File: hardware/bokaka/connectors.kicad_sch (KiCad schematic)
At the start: 3 parts, among them J1 USB_C_Receptacle_USB2.0_16P

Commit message: Adding rest of design and pdf
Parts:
- added J2: Tap Connector, symbol Connector:Conn_01x05_Pin
- added J3: SWD Connector, Connector:Tag-Connect_TC2030-IDC-NL_2x03_P1.27mm_Vertical, symbol Connector:Conn_ARM_SWD_TagConnect_TC2030-NL
- added J4: Conn_01x02_Pin, symbol Connector:Conn_01x02_Pin
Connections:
- net GND: now also J2.1 (Pin_1), J3.5 (GND)
- new net +3V3: J3.1 (VCC)
- new net I2C_SCL: J4.2 (Pin_2)
- new net I2C_SDA: J4.1 (Pin_1)
- new net SWD_SWCLK: J3.4 (SWCLK)
- new net SWD_SWDIO: J3.2 (SWDIO)
- new net TAP_DATA: J2.2 (Pin_2)
- new net TAP_DETECT: J2.3 (Pin_3)
- new net UART_RX: J2.4 (Pin_4)
- new net UART_TX: J2.5 (Pin_5)
- new net ~{RESET}: J3.3 (~{RESET})
- no-connect marks 2 -> 3

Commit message: Finalize design before pcb
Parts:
- removed J2: Tap Connector, symbol Connector:Conn_01x05_Pin
- added J2: Conn_01x02_Pin, symbol Connector:Conn_01x02_Pin
- added J5, J6: Conn_01x03_Pin, symbol Connector:Conn_01x03_Pin
- added U4: PESD5V0L4UG_115, Footprints:SOT65P210X110-5N, symbol Symbols:PESD5V0L4UG_115
- J3: footprint Connector:Tag-Connect_TC2030-IDC-NL_2x03_P1.27mm_Vertical -> Footprints:Edge_Connect_6
- R2, R3: footprint (none) -> Resistor_SMD:R_0402_1005Metric
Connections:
- net GND: now also J5.1 (Pin_1), J6.3 (Pin_3), U4.2
- net TAP_DATA: now also J5.3 (Pin_3), J6.1 (Pin_1), U4.4
- net TAP_DETECT: now also J5.2 (Pin_2), J6.2 (Pin_2), U4.5
- net UART_RX: now also J2.1 (Pin_1)
- net UART_TX: now also J2.2 (Pin_2)
- net USB_D-: now also U4.1, U4.3
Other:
- note added: "ESD Protection"
- moved on the sheet: J3

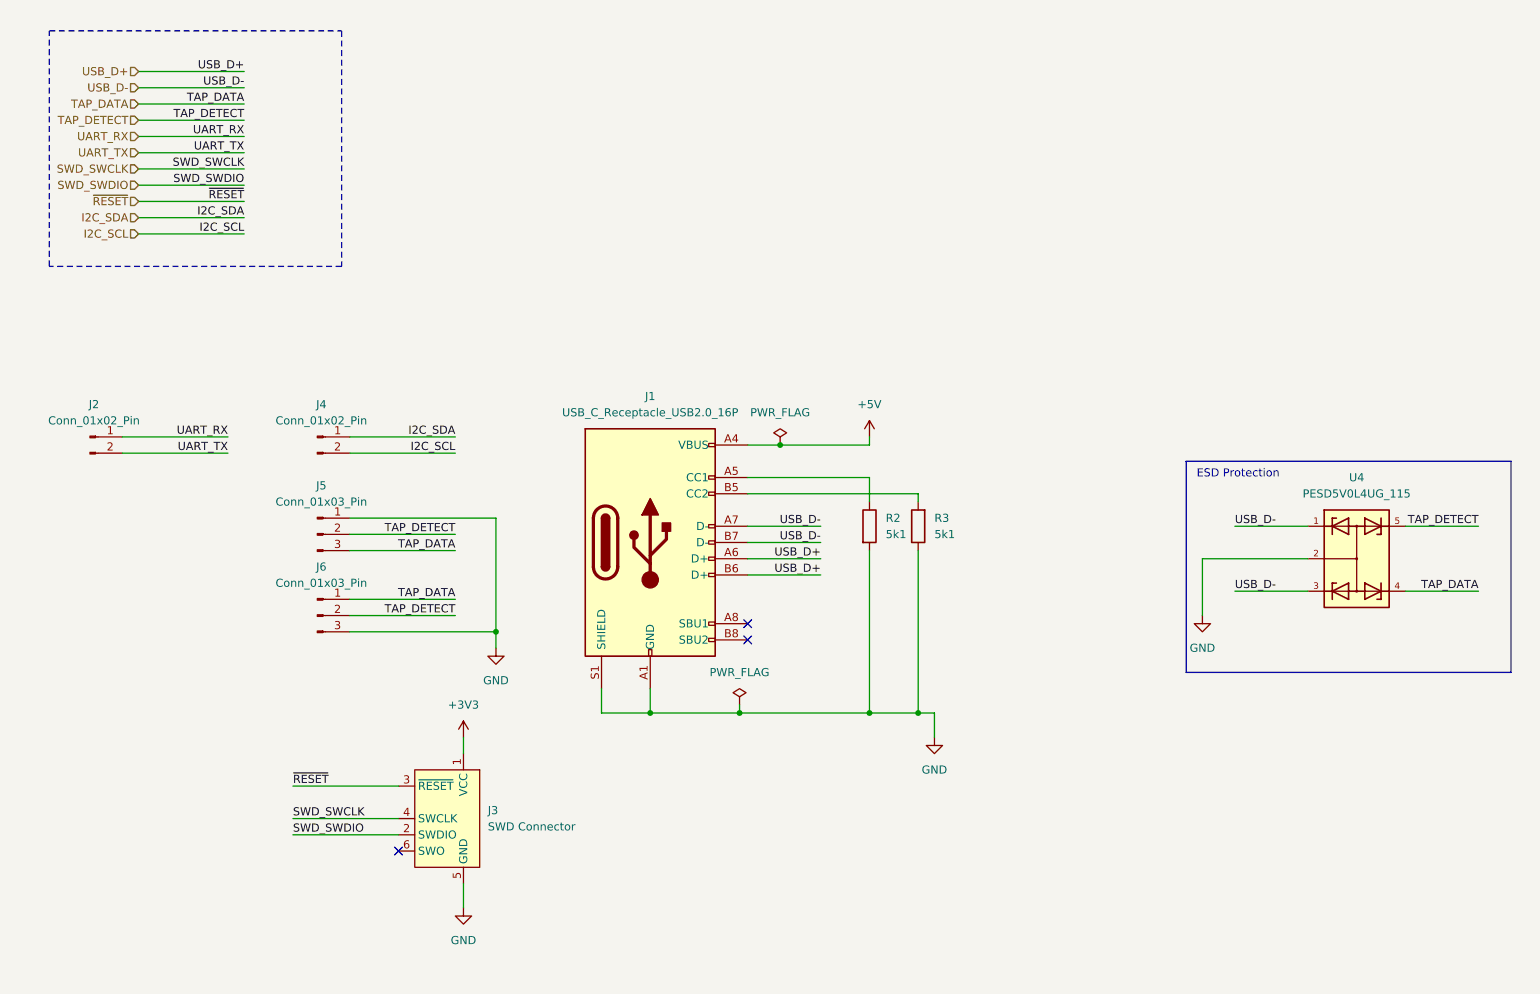
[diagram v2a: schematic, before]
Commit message: footprint asignment
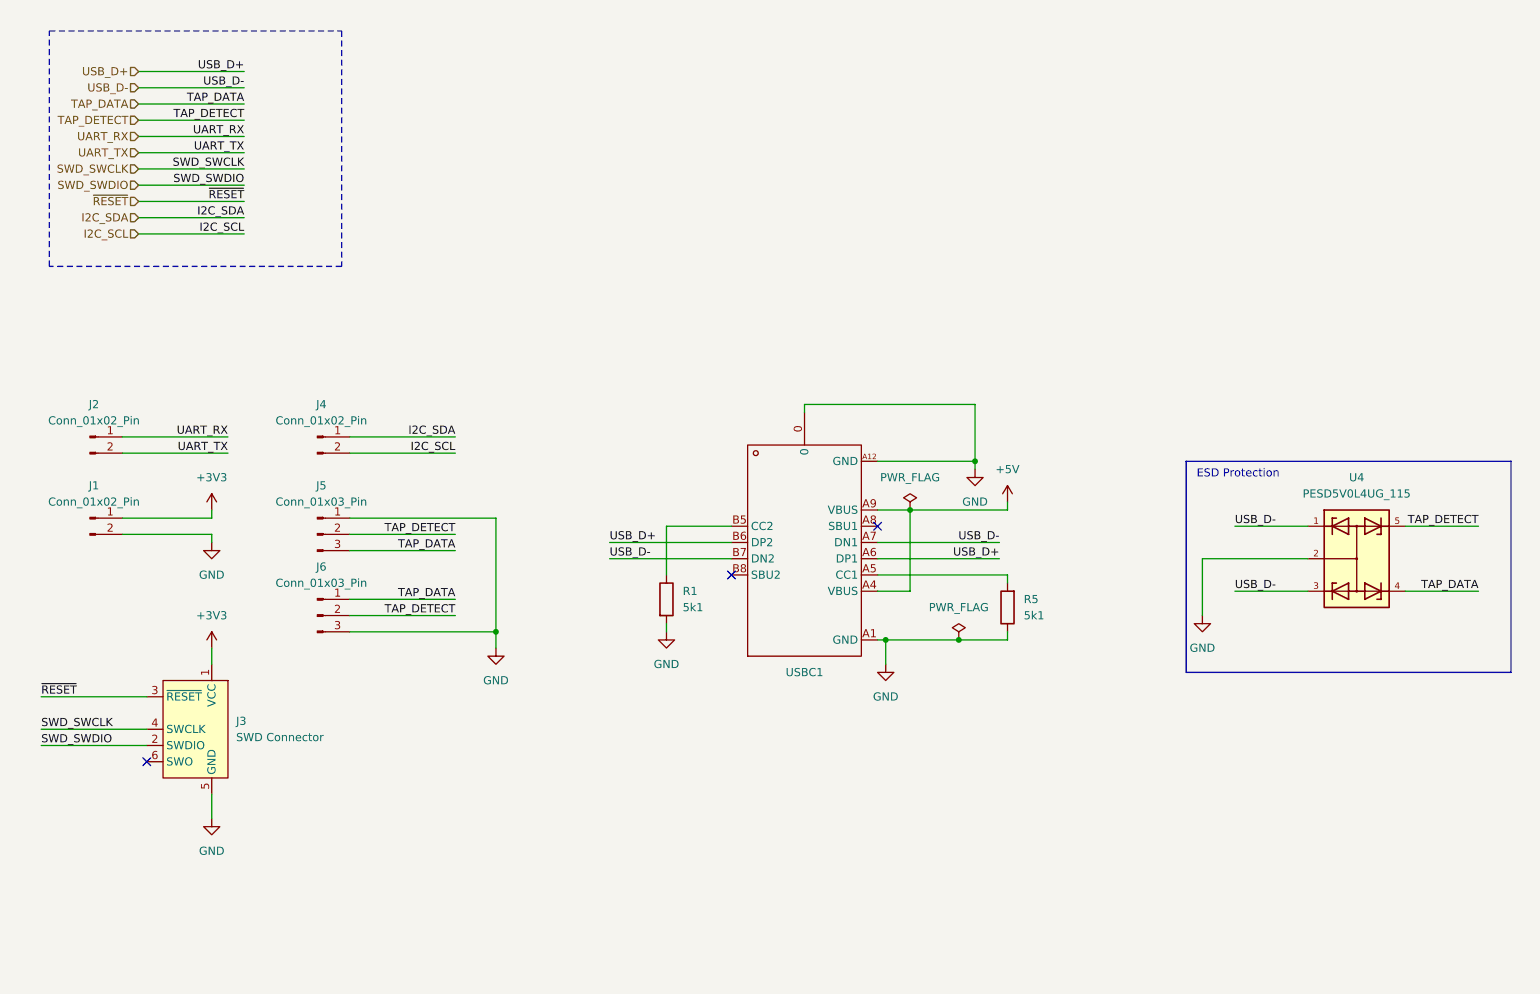
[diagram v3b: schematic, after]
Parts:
- removed J1: USB_C_Receptacle_USB2.0_16P, symbol Connector:USB_C_Receptacle_USB2.0_16P
- removed R2, R3: 5k1, Resistor_SMD:R_0402_1005Metric, symbol Device:R
- added J1: Conn_01x02_Pin, Connector_PinHeader_2.54mm:PinHeader_1x02_P2.54mm_Vertical, symbol Connector:Conn_01x02_Pin
- added R1, R5: 5k1, Resistor_SMD:R_0402_1005Metric, symbol Device:R
- added USBC1: ~, EasyEDA_Lib:USB-C-SMD_TYPE-C-USB-17, symbol Symbols:USB3.1C16PFSMT
- J2, J4: footprint (none) -> Connector_PinHeader_2.54mm:PinHeader_1x02_P2.54mm_Vertical
- J5, J6: footprint (none) -> Connector_PinHeader_2.54mm:PinHeader_1x03_P2.54mm_Vertical
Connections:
- net +3V3: now also J1.1 (Pin_1)
- net +5V: now also USBC1.A4 (VBUS), USBC1.A9 (VBUS)
- net GND: now also J1.2 (Pin_2), R1.2, R5.1, USBC1.0, USBC1.A1 (GND), USBC1.A12 (GND)
- net USB_D+: now also USBC1.A6 (DP1), USBC1.B6 (DP2)
- net USB_D-: now also USBC1.A7 (DN1), USBC1.B7 (DN2)
- new net: R1.1, USBC1.B5 (CC2)
- new net: R5.2, USBC1.A5 (CC1)
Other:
- moved on the sheet: J3

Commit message: schematic update
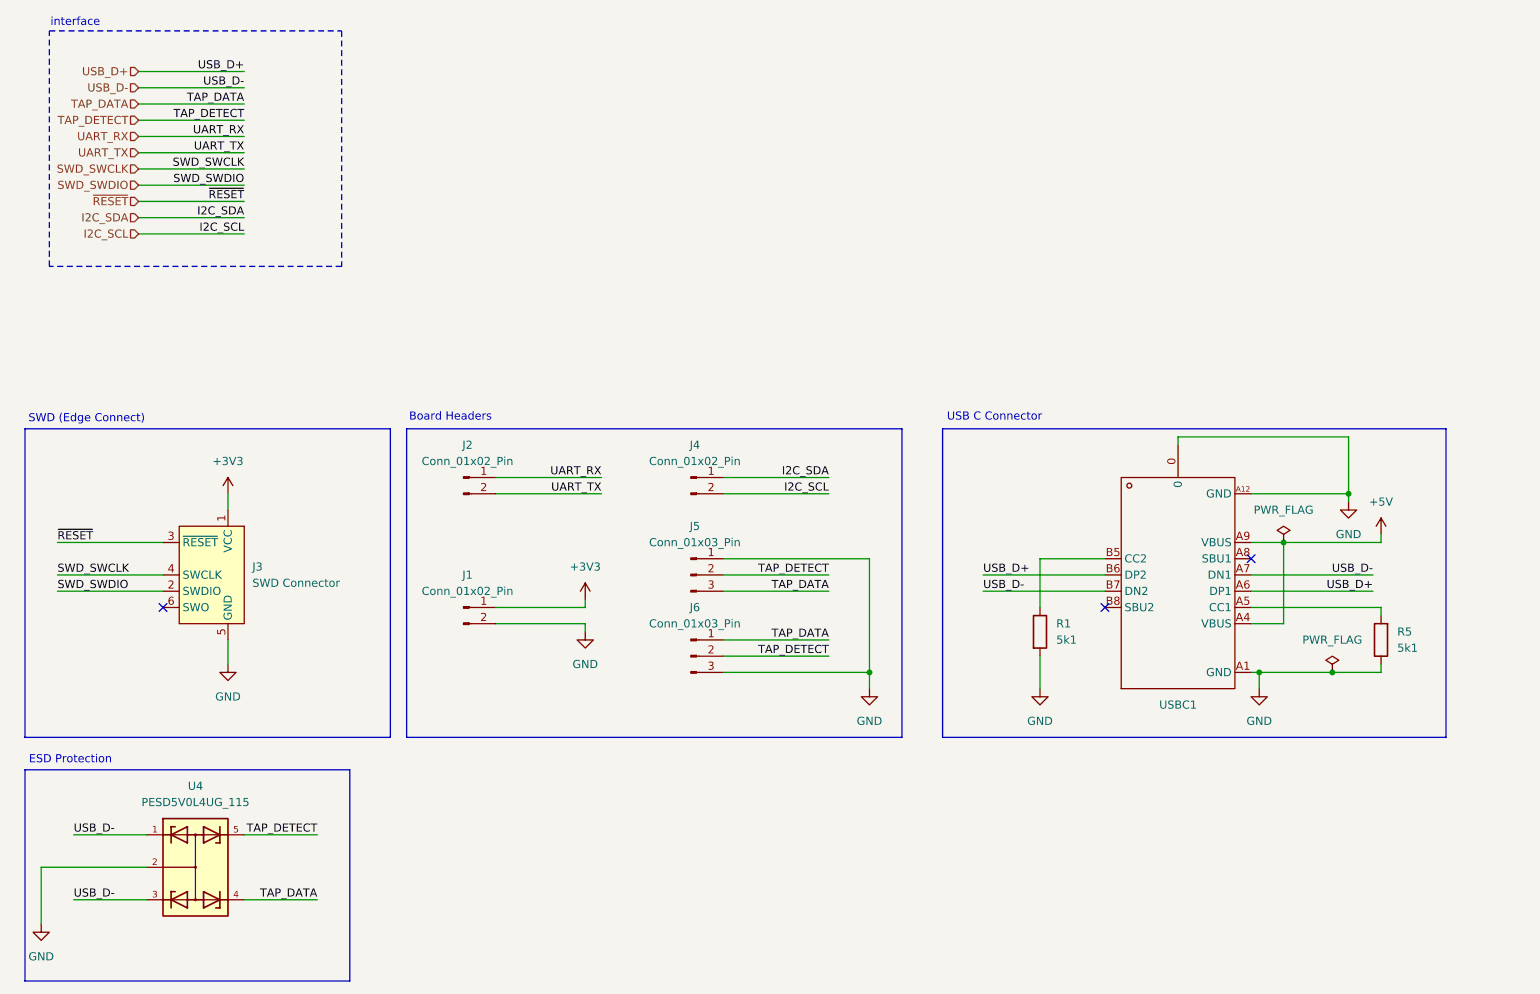
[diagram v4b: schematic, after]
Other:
- note added: "Board Headers"
- note added: "SWD (Edge Connect)"
- note added: "USB C Connector"
- note added: "interface"
- moved on the sheet: J1, J2, J3, J4, J5, J6, R1, R5, U4, USBC1

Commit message: Devkit Production Ready
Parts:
- removed J4: Conn_01x02_Pin, Connector_PinHeader_2.54mm:PinHeader_1x02_P2.54mm_Vertical, symbol Connector:Conn_01x02_Pin
- added F1: 500mA, Fuse:Fuse_1206_3216Metric, symbol Device:Polyfuse
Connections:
- net +5V: now also F1.2; no longer USBC1.A4 (VBUS), USBC1.A9 (VBUS)
- net TAP_DATA: now also J5.2 (Pin_2), J6.2 (Pin_2); no longer J5.3 (Pin_3), J6.1 (Pin_1)
- net TAP_DETECT: now also J5.3 (Pin_3), J6.1 (Pin_1); no longer J5.2 (Pin_2), J6.2 (Pin_2)
- net USB_D+: now also U4.3
- net USB_D-: no longer U4.3
- new net: F1.1, USBC1.A4 (VBUS), USBC1.A9 (VBUS)
